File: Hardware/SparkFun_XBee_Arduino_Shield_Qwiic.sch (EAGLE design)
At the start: 89 parts, among them J4 QWIIC_RIGHT_ANGLE, Q1 3.1A/30V/105mΩ, Q2 3.1A/30V/105mΩ, Q3 3.1A/30V/105mΩ, Q4 5.8A/30V/35mΩ, Q5 20V/4.2A/52mΩ/1.4W, U1 FSUSB30MUX_MSOP10, U2 AP63203, U3 ESD Diode, U4 FT231XS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

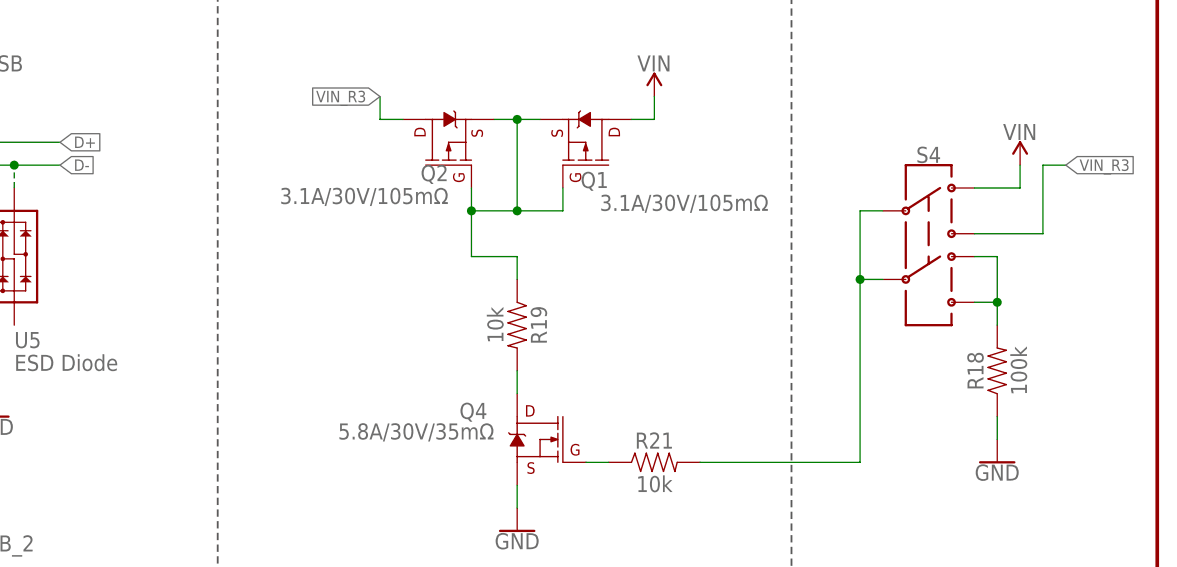
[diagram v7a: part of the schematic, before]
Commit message: Replaces the PCHAN with a more suitable one
* Routing improvements
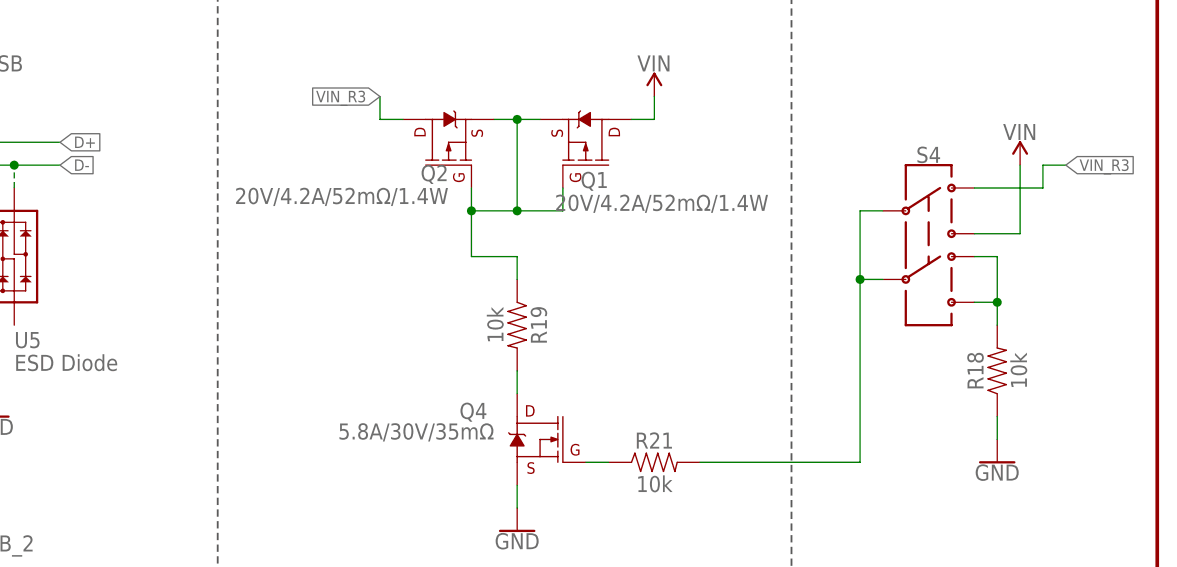
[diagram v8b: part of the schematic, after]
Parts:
- Q1, Q2: value 3.1A/30V/105mΩ -> 20V/4.2A/52mΩ/1.4W; device SparkFun-DiscreteSemi:MOSFET_PCH-DMG2307L -> SparkFun-DiscreteSemi:MOSFET_PCH-DMG2305UX-7
- R18: value 100k -> 10k; device SparkFun-Resistors:100KOHM-0603-1/10W-1% -> SparkFun-Resistors:10KOHM-0603-1/10W-1%
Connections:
- net OFF_VIN renamed OFF_XB
- net VIN: now also S4.1; no longer S4.3
- net VIN_R3: now also S4.3; no longer S4.1
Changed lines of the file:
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@@
 <part name="IO4" library="SparkFun-Jumpers" deviceset="JUMPER-SMT_2_NC_TRACE" device="_SILK" package3d_urn="urn:adsk.eagle:package:39281/1"/>
 <part name="S4" library="SparkFun-Switches" deviceset="SWITCH-DPDT" device="-SMD-AYZ0202"/>
-<part name="R18" library="SparkFun-Resistors" deviceset="100KOHM" device="-0603-1/10W-1%" value="100k"/>
+<part name="R18" library="SparkFun-Resistors" deviceset="10KOHM" device="-0603-1/10W-1%" value="10k"/>
 <part name="GND42" library="SparkFun-PowerSymbols" deviceset="GND" device=""/>
 <part name="SUPPLY34" library="SparkFun-PowerSymbols" deviceset="VIN" device=""/>
@@
 <part name="R20" library="SparkFun-Resistors" deviceset="10KOHM" device="-0603-1/10W-1%" value="10k"/>
 <part name="GND44" library="SparkFun-PowerSymbols" deviceset="GND" device=""/>
-<part name="Q1" library="SparkFun-DiscreteSemi" deviceset="MOSFET_PCH" device="-DMG2307L" value="3.1A/30V/105mΩ"/>
-<part name="Q2" library="SparkFun-DiscreteSemi" deviceset="MOSFET_PCH" device="-DMG2307L" value="3.1A/30V/105mΩ"/>
+<part name="Q1" library="SparkFun-DiscreteSemi" deviceset="MOSFET_PCH" device="-DMG2305UX-7" value="20V/4.2A/52mΩ/1.4W"/>
+<part name="Q2" library="SparkFun-DiscreteSemi" deviceset="MOSFET_PCH" device="-DMG2305UX-7" value="20V/4.2A/52mΩ/1.4W"/>
 <part name="SUPPLY2" library="SparkFun-PowerSymbols" deviceset="VIN" device=""/>
 <part name="Q4" library="SparkFun-DiscreteSemi" deviceset="MOSFET-NCH" device="-AO3404A" value="5.8A/30V/35mΩ"/>
@@
 </segment>
 <segment>
-<pinref part="SUPPLY34" gate="G$1" pin="VIN"/>
-<pinref part="S4" gate="G$1" pin="3"/>
-<wire x1="416.56" y1="243.84" x2="416.56" y2="246.38" width="0.1524" layer="91"/>
-<wire x1="411.48" y1="243.84" x2="416.56" y2="243.84" width="0.1524" layer="91"/>
-</segment>
-<segment>
 <pinref part="Q1" gate="G$1" pin="D"/>
 <wire x1="373.38" y1="251.46" x2="375.92" y2="251.46" width="0.1524" layer="91"/>
 <wire x1="375.92" y1="251.46" x2="375.92" y2="254" width="0.1524" layer="91"/>
 <pinref part="SUPPLY2" gate="G$1" pin="VIN"/>
+</segment>
+<segment>
+<pinref part="S4" gate="G$1" pin="1"/>
+<wire x1="411.48" y1="238.76" x2="416.56" y2="238.76" width="0.1524" layer="91"/>
+<pinref part="SUPPLY34" gate="G$1" pin="VIN"/>
+<wire x1="416.56" y1="246.38" x2="416.56" y2="238.76" width="0.1524" layer="91"/>
 </segment>
 </net>
@@
 </segment>
 </net>
-<net name="OFF_VIN" class="0">
+<net name="OFF_XB" class="0">
 <segment>
 <pinref part="S4" gate="G$1" pin="6"/>
@@
 </segment>
 <segment>
-<pinref part="S4" gate="G$1" pin="1"/>
-<wire x1="411.48" y1="238.76" x2="419.1" y2="238.76" width="0.1524" layer="91"/>
-<wire x1="419.1" y1="238.76" x2="419.1" y2="246.38" width="0.1524" layer="91"/>
-<wire x1="419.1" y1="246.38" x2="421.64" y2="246.38" width="0.1524" layer="91"/>
-<label x="421.64" y="246.38" size="1.27" layer="95" font="vector" xref="yes"/>
-</segment>
-<segment>
 <pinref part="B1" gate="G$1" pin="VIN"/>
 <wire x1="144.78" y1="109.22" x2="139.7" y2="109.22" width="0.1524" layer="91"/>
@@
 <label x="142.24" y="142.24" size="1.27" layer="95" font="vector" xref="yes"/>
 </segment>
-</net>
+<segment>
+<pinref part="S4" gate="G$1" pin="3"/>
+<wire x1="411.48" y1="243.84" x2="419.1" y2="243.84" width="0.1524" layer="91"/>
+<wire x1="419.1" y1="246.38" x2="421.64" y2="246.38" width="0.1524" layer="91"/>
+<label x="421.64" y="246.38" size="1.27" layer="95" font="vector" xref="yes"/>
+<wire x1="419.1" y1="243.84" x2="419.1" y2="246.38" width="0.1524" layer="91"/>
+</segment>
+</net>
